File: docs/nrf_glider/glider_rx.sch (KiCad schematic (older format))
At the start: 8 parts

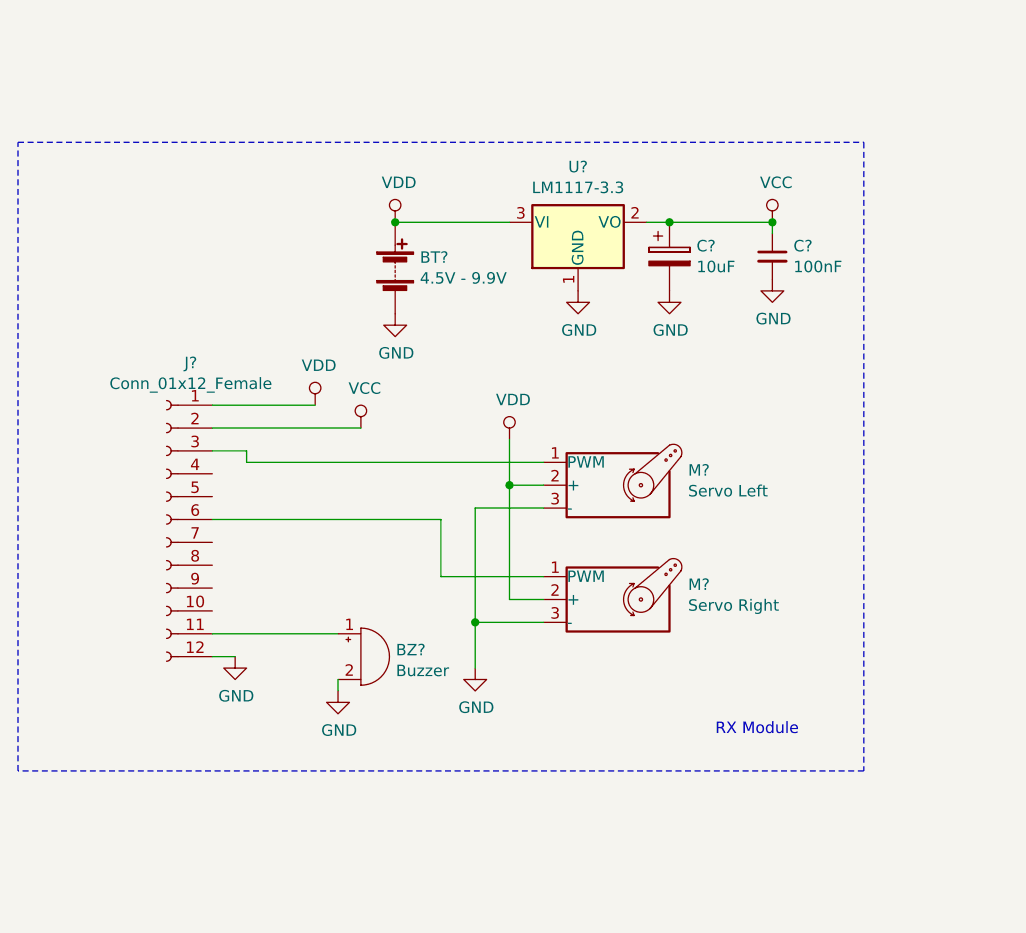
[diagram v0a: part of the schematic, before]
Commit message: added hierarchical sheets and labels
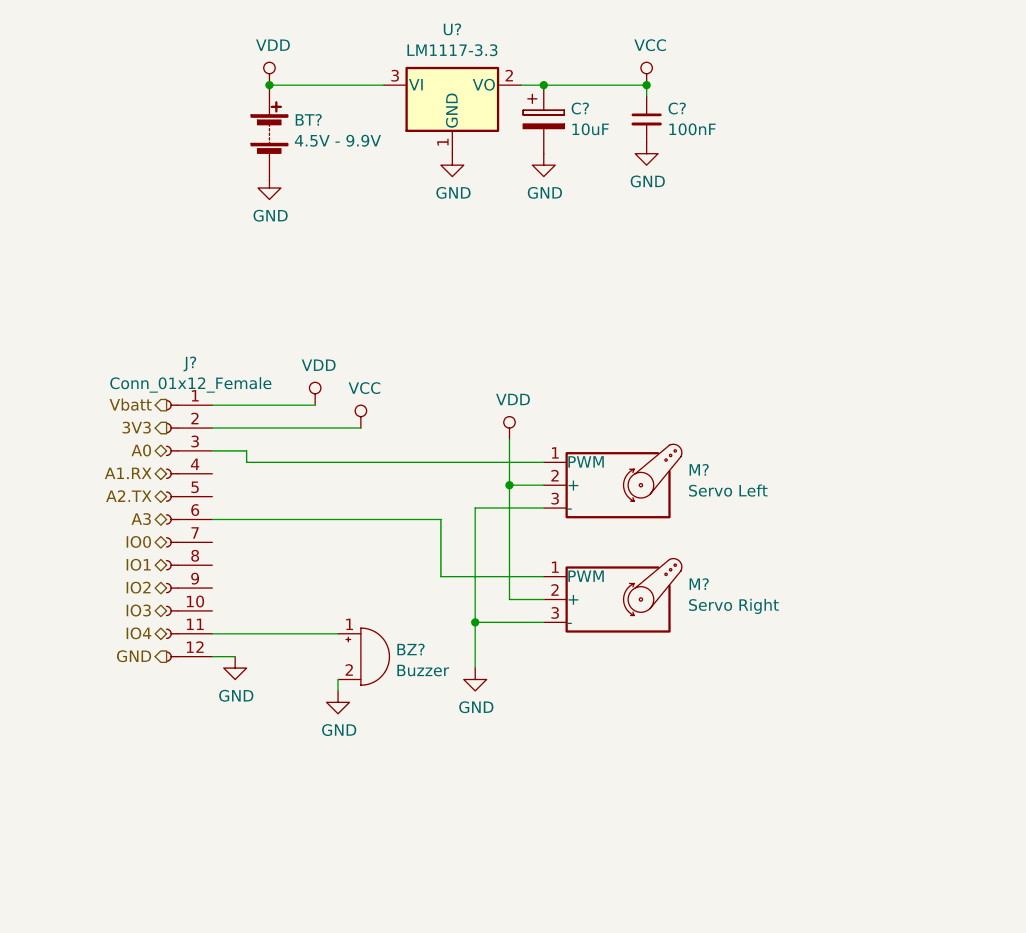
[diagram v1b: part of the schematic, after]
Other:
- note removed: "RX Module"
- moved on the sheet: BT?, C?, U?
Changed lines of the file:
@@
 $Descr A4 11693 8268
 encoding utf-8
-Sheet 4 4
+Sheet 1 5
 Title ""
 Date ""
@@
 L Regulator_Linear:LM1117-3.3 U?
 U 1 1 5BCECE85
-P 5050 2450
-F 0 "U?" H 5050 2692 50  0000 C CNN
-F 1 "LM1117-3.3" H 5050 2601 50  0000 C CNN
-F 2 "" H 5050 2450 50  0001 C CNN
-F 3 "http://www.ti.com/lit/ds/symlink/lm1117.pdf" H 5050 2450 50  0001 C CNN
-	1    5050 2450
+P 4500 1850
+F 0 "U?" H 4500 2092 50  0000 C CNN
+F 1 "LM1117-3.3" H 4500 2001 50  0000 C CNN
+F 2 "" H 4500 1850 50  0001 C CNN
+F 3 "http://www.ti.com/lit/ds/symlink/lm1117.pdf" H 4500 1850 50  0001 C CNN
+	1    4500 1850
 	1    0    0    -1
 $EndComp
@@
 L power:GND #PWR?
 U 1 1 5BCED801
-P 5050 2750
-F 0 "#PWR?" H 5050 2500 50  0001 C CNN
-F 1 "GND" H 5055 2577 50  0000 C CNN
-F 2 "" H 5050 2750 50  0001 C CNN
-F 3 "" H 5050 2750 50  0001 C CNN
-	1    5050 2750
+P 4500 2150
+F 0 "#PWR?" H 4500 1900 50  0001 C CNN
+F 1 "GND" H 4505 1977 50  0000 C CNN
+F 2 "" H 4500 2150 50  0001 C CNN
+F 3 "" H 4500 2150 50  0001 C CNN
+	1    4500 2150
 	1    0    0    -1
 $EndComp
@@
 L Device:Battery BT?
 U 1 1 5BCED8B9
-P 4250 2650
-F 0 "BT?" H 4358 2696 50  0000 L CNN
-F 1 "4.5V - 9.9V" H 4358 2605 50  0000 L CNN
-F 2 "Connector_PinHeader_2.54mm:PinHeader_1x02_P2.54mm_Vertical" V 4250 2710 50  0001 C CNN
-F 3 "~" V 4250 2710 50  0001 C CNN
-	1    4250 2650
-	1    0    0    -1
-$EndComp
-Wire Wire Line
-	4250 2450 4750 2450
+P 3700 2050
+F 0 "BT?" H 3808 2096 50  0000 L CNN
+F 1 "4.5V - 9.9V" H 3808 2005 50  0000 L CNN
+F 2 "Connector_PinHeader_2.54mm:PinHeader_1x02_P2.54mm_Vertical" V 3700 2110 50  0001 C CNN
+F 3 "~" V 3700 2110 50  0001 C CNN
+	1    3700 2050
+	1    0    0    -1
+$EndComp
+Wire Wire Line
+	3700 1850 4200 1850
 $Comp
 L power:GND #PWR?
 U 1 1 5BCED983
-P 4250 2850
-F 0 "#PWR?" H 4250 2600 50  0001 C CNN
-F 1 "GND" H 4255 2677 50  0000 C CNN
-F 2 "" H 4250 2850 50  0001 C CNN
-F 3 "" H 4250 2850 50  0001 C CNN
-	1    4250 2850
+P 3700 2250
+F 0 "#PWR?" H 3700 2000 50  0001 C CNN
+F 1 "GND" H 3705 2077 50  0000 C CNN
+F 2 "" H 3700 2250 50  0001 C CNN
+F 3 "" H 3700 2250 50  0001 C CNN
+	1    3700 2250
 	1    0    0    -1
 $EndComp
@@
 L power:VCC #PWR?
 U 1 1 5BCED9FA
-P 5900 2450
-F 0 "#PWR?" H 5900 2300 50  0001 C CNN
-F 1 "VCC" H 5917 2623 50  0000 C CNN
-F 2 "" H 5900 2450 50  0001 C CNN
-F 3 "" H 5900 2450 50  0001 C CNN
-	1    5900 2450
+P 5350 1850
+F 0 "#PWR?" H 5350 1700 50  0001 C CNN
+F 1 "VCC" H 5367 2023 50  0000 C CNN
+F 2 "" H 5350 1850 50  0001 C CNN
+F 3 "" H 5350 1850 50  0001 C CNN
+	1    5350 1850
 	1    0    0    -1
 $EndComp
@@
 L Device:C_Small C?
 U 1 1 5BCEDC62
-P 5900 2600
-F 0 "C?" H 5992 2646 50  0000 L CNN
-F 1 "100nF" H 5992 2555 50  0000 L CNN
-F 2 "Capacitor_THT:C_Disc_D5.0mm_W2.5mm_P5.00mm" H 5900 2600 50  0001 C CNN
-F 3 "~" H 5900 2600 50  0001 C CNN
-	1    5900 2600
+P 5350 2000
+F 0 "C?" H 5442 2046 50  0000 L CNN
+F 1 "100nF" H 5442 1955 50  0000 L CNN
+F 2 "Capacitor_THT:C_Disc_D5.0mm_W2.5mm_P5.00mm" H 5350 2000 50  0001 C CNN
+F 3 "~" H 5350 2000 50  0001 C CNN
+	1    5350 2000
 	1    0    0    -1
 $EndComp
@@
 L Device:CP C?
 U 1 1 5BCEDD9D
-P 5450 2600
-F 0 "C?" H 5568 2646 50  0000 L CNN
-F 1 "10uF" H 5568 2555 50  0000 L CNN
-F 2 "Capacitor_THT:CP_Radial_D8.0mm_P2.50mm" H 5488 2450 50  0001 C CNN
-F 3 "~" H 5450 2600 50  0001 C CNN
-	1    5450 2600
+P 4900 2000
+F 0 "C?" H 5018 2046 50  0000 L CNN
+F 1 "10uF" H 5018 1955 50  0000 L CNN
+F 2 "Capacitor_THT:CP_Radial_D8.0mm_P2.50mm" H 4938 1850 50  0001 C CNN
+F 3 "~" H 4900 2000 50  0001 C CNN
+	1    4900 2000
 	1    0    0    -1
 $EndComp
@@
 L power:GND #PWR?
 U 1 1 5BCEDF2F
-P 5450 2750
-F 0 "#PWR?" H 5450 2500 50  0001 C CNN
-F 1 "GND" H 5455 2577 50  0000 C CNN
-F 2 "" H 5450 2750 50  0001 C CNN
-F 3 "" H 5450 2750 50  0001 C CNN
-	1    5450 2750
+P 4900 2150
+F 0 "#PWR?" H 4900 1900 50  0001 C CNN
+F 1 "GND" H 4905 1977 50  0000 C CNN
+F 2 "" H 4900 2150 50  0001 C CNN
+F 3 "" H 4900 2150 50  0001 C CNN
+	1    4900 2150
 	1    0    0    -1
 $EndComp
@@
 L power:GND #PWR?
 U 1 1 5BCEDF6D
-P 5900 2700
-F 0 "#PWR?" H 5900 2450 50  0001 C CNN
-F 1 "GND" H 5905 2527 50  0000 C CNN
-F 2 "" H 5900 2700 50  0001 C CNN
-F 3 "" H 5900 2700 50  0001 C CNN
-	1    5900 2700
-	1    0    0    -1
-$EndComp
-Wire Wire Line
-	5350 2450 5450 2450
+P 5350 2100
+F 0 "#PWR?" H 5350 1850 50  0001 C CNN
+F 1 "GND" H 5355 1927 50  0000 C CNN
+F 2 "" H 5350 2100 50  0001 C CNN
+F 3 "" H 5350 2100 50  0001 C CNN
+	1    5350 2100
+	1    0    0    -1
+$EndComp
+Wire Wire Line
+	4800 1850 4900 1850
 $Comp
 L power:VDD #PWR?
 U 1 1 5BCF6415
-P 4250 2450
-F 0 "#PWR?" H 4250 2300 50  0001 C CNN
-F 1 "VDD" H 4267 2623 50  0000 C CNN
-F 2 "" H 4250 2450 50  0001 C CNN
-F 3 "" H 4250 2450 50  0001 C CNN
-	1    4250 2450
-	1    0    0    -1
-$EndComp
-Connection ~ 4250 2450
-Wire Wire Line
-	5900 2450 5900 2500
-Connection ~ 5900 2450
-Wire Wire Line
-	5450 2450 5900 2450
-Connection ~ 5450 2450
+P 3700 1850
+F 0 "#PWR?" H 3700 1700 50  0001 C CNN
+F 1 "VDD" H 3717 2023 50  0000 C CNN
+F 2 "" H 3700 1850 50  0001 C CNN
+F 3 "" H 3700 1850 50  0001 C CNN
+	1    3700 1850
+	1    0    0    -1
+$EndComp
+Connection ~ 3700 1850
+Wire Wire Line
+	5350 1850 5350 1900
+Connection ~ 5350 1850
+Wire Wire Line
+	4900 1850 5350 1850
+Connection ~ 4900 1850
 $Comp
 L Connector:Conn_01x12_Female J?
@@
 	1    0    0    -1
 $EndComp
-Wire Notes Line
-	2600 2100 6300 2100
-Wire Notes Line
-	6300 2100 6300 4850
-Wire Notes Line
-	6300 4850 2600 4850
-Wire Notes Line
-	2600 4850 2600 2100
-Text Notes 5650 4700 0    50   ~ 0
-RX Module
 Wire Wire Line
 	3450 3450 3600 3450
@@
 Text Notes 10300 7350 0    50   ~ 0
 created by Toby Kurien
+Text HLabel 3250 3250 0    50   Output ~ 0
+Vbatt
+Text HLabel 3250 3350 0    50   Output ~ 0
+3V3
+Text HLabel 3250 3450 0    50   BiDi ~ 0
+A0
+Text HLabel 3250 3550 0    50   BiDi ~ 0
+A1.RX
+Text HLabel 3250 3650 0    50   BiDi ~ 0
+A2.TX
+Text HLabel 3250 3750 0    50   BiDi ~ 0
+A3
+Text HLabel 3250 3850 0    50   BiDi ~ 0
+IO0
+Text HLabel 3250 3950 0    50   BiDi ~ 0
+IO1
+Text HLabel 3250 4050 0    50   BiDi ~ 0
+IO2
+Text HLabel 3250 4150 0    50   BiDi ~ 0
+IO3
+Text HLabel 3250 4250 0    50   BiDi ~ 0
+IO4
+Text HLabel 3250 4350 0    50   Output ~ 0
+GND
 $EndSCHEMATC

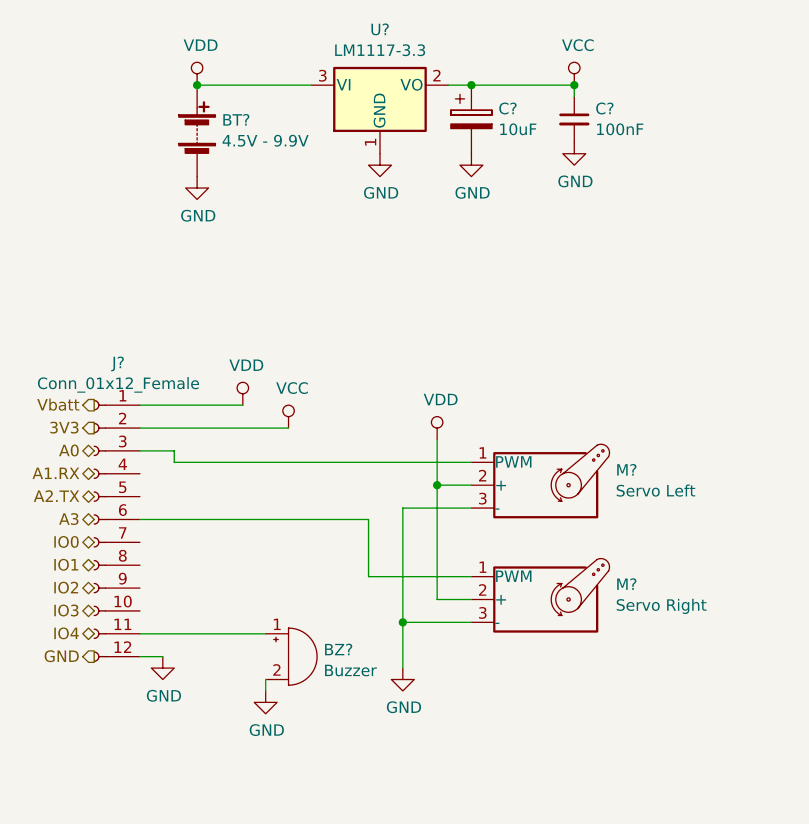
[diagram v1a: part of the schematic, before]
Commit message: remove and ignore bak files
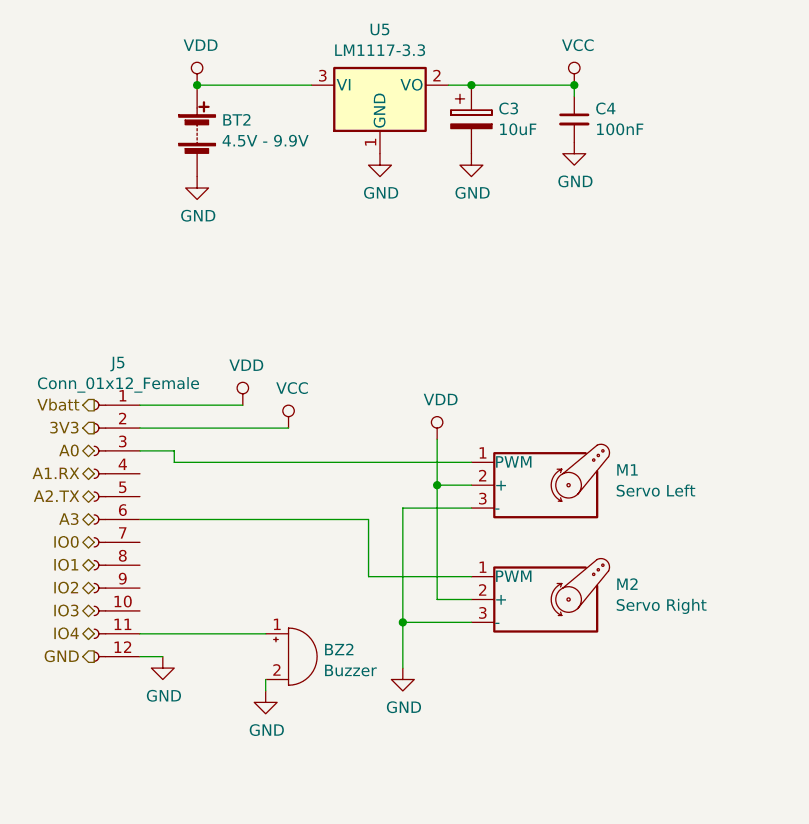
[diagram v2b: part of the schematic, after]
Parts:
- gave numbers to parts that had none: 8
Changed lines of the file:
@@
 $EndDescr
 $Comp
-L Regulator_Linear:LM1117-3.3 U?
+L Regulator_Linear:LM1117-3.3 U5
 U 1 1 5BCECE85
 P 4500 1850
-F 0 "U?" H 4500 2092 50  0000 C CNN
+F 0 "U5" H 4500 2092 50  0000 C CNN
 F 1 "LM1117-3.3" H 4500 2001 50  0000 C CNN
 F 2 "" H 4500 1850 50  0001 C CNN
@@
 $EndComp
 $Comp
-L power:GND #PWR?
+L power:GND #PWR0129
 U 1 1 5BCED801
 P 4500 2150
-F 0 "#PWR?" H 4500 1900 50  0001 C CNN
+F 0 "#PWR0129" H 4500 1900 50  0001 C CNN
 F 1 "GND" H 4505 1977 50  0000 C CNN
 F 2 "" H 4500 2150 50  0001 C CNN
@@
 $EndComp
 $Comp
-L Device:Battery BT?
+L Device:Battery BT2
 U 1 1 5BCED8B9
 P 3700 2050
-F 0 "BT?" H 3808 2096 50  0000 L CNN
+F 0 "BT2" H 3808 2096 50  0000 L CNN
 F 1 "4.5V - 9.9V" H 3808 2005 50  0000 L CNN
 F 2 "Connector_PinHeader_2.54mm:PinHeader_1x02_P2.54mm_Vertical" V 3700 2110 50  0001 C CNN
@@
 	3700 1850 4200 1850
 $Comp
-L power:GND #PWR?
+L power:GND #PWR0130
 U 1 1 5BCED983
 P 3700 2250
-F 0 "#PWR?" H 3700 2000 50  0001 C CNN
+F 0 "#PWR0130" H 3700 2000 50  0001 C CNN
 F 1 "GND" H 3705 2077 50  0000 C CNN
 F 2 "" H 3700 2250 50  0001 C CNN
@@
 $EndComp
 $Comp
-L power:VCC #PWR?
+L power:VCC #PWR0131
 U 1 1 5BCED9FA
 P 5350 1850
-F 0 "#PWR?" H 5350 1700 50  0001 C CNN
+F 0 "#PWR0131" H 5350 1700 50  0001 C CNN
 F 1 "VCC" H 5367 2023 50  0000 C CNN
 F 2 "" H 5350 1850 50  0001 C CNN
@@
 $EndComp
 $Comp
-L Device:C_Small C?
+L Device:C_Small C4
 U 1 1 5BCEDC62
 P 5350 2000
-F 0 "C?" H 5442 2046 50  0000 L CNN
+F 0 "C4" H 5442 2046 50  0000 L CNN
 F 1 "100nF" H 5442 1955 50  0000 L CNN
 F 2 "Capacitor_THT:C_Disc_D5.0mm_W2.5mm_P5.00mm" H 5350 2000 50  0001 C CNN
@@
 $EndComp
 $Comp
-L Device:CP C?
+L Device:CP C3
 U 1 1 5BCEDD9D
 P 4900 2000
-F 0 "C?" H 5018 2046 50  0000 L CNN
+F 0 "C3" H 5018 2046 50  0000 L CNN
 F 1 "10uF" H 5018 1955 50  0000 L CNN
 F 2 "Capacitor_THT:CP_Radial_D8.0mm_P2.50mm" H 4938 1850 50  0001 C CNN
@@
 $EndComp
 $Comp
-L power:GND #PWR?
+L power:GND #PWR0132
 U 1 1 5BCEDF2F
 P 4900 2150
-F 0 "#PWR?" H 4900 1900 50  0001 C CNN
+F 0 "#PWR0132" H 4900 1900 50  0001 C CNN
 F 1 "GND" H 4905 1977 50  0000 C CNN
 F 2 "" H 4900 2150 50  0001 C CNN
@@
 $EndComp
 $Comp
-L power:GND #PWR?
+L power:GND #PWR0133
 U 1 1 5BCEDF6D
 P 5350 2100
-F 0 "#PWR?" H 5350 1850 50  0001 C CNN
+F 0 "#PWR0133" H 5350 1850 50  0001 C CNN
 F 1 "GND" H 5355 1927 50  0000 C CNN
 F 2 "" H 5350 2100 50  0001 C CNN
@@
 	4800 1850 4900 1850
 $Comp
-L power:VDD #PWR?
+L power:VDD #PWR0134
 U 1 1 5BCF6415
 P 3700 1850
-F 0 "#PWR?" H 3700 1700 50  0001 C CNN
+F 0 "#PWR0134" H 3700 1700 50  0001 C CNN
 F 1 "VDD" H 3717 2023 50  0000 C CNN
 F 2 "" H 3700 1850 50  0001 C CNN
@@
 Connection ~ 4900 1850
 $Comp
-L Connector:Conn_01x12_Female J?
+L Connector:Conn_01x12_Female J5
 U 1 1 5BD137AB
 P 3250 3750
-F 0 "J?" H 3144 4435 50  0000 C CNN
+F 0 "J5" H 3144 4435 50  0000 C CNN
 F 1 "Conn_01x12_Female" H 3144 4344 50  0000 C CNN
 F 2 "Connector_PinHeader_2.54mm:PinHeader_1x12_P2.54mm_Vertical" H 3250 3750 50  0001 C CNN
@@
 $EndComp
 $Comp
-L power:VDD #PWR?
+L power:VDD #PWR0135
 U 1 1 5BD1962D
 P 3900 3250
-F 0 "#PWR?" H 3900 3100 50  0001 C CNN
+F 0 "#PWR0135" H 3900 3100 50  0001 C CNN
 F 1 "VDD" H 3917 3423 50  0000 C CNN
 F 2 "" H 3900 3250 50  0001 C CNN
@@
 	3900 3250 3450 3250
 $Comp
-L power:VCC #PWR?
+L power:VCC #PWR0136
 U 1 1 5BD1B4CC
 P 4100 3350
-F 0 "#PWR?" H 4100 3200 50  0001 C CNN
+F 0 "#PWR0136" H 4100 3200 50  0001 C CNN
 F 1 "VCC" H 4117 3523 50  0000 C CNN
 F 2 "" H 4100 3350 50  0001 C CNN
@@
 	3450 3350 4100 3350
 $Comp
-L power:GND #PWR?
+L power:GND #PWR0137
 U 1 1 5BD1F411
 P 3550 4350
-F 0 "#PWR?" H 3550 4100 50  0001 C CNN
+F 0 "#PWR0137" H 3550 4100 50  0001 C CNN
 F 1 "GND" H 3555 4177 50  0000 C CNN
 F 2 "" H 3550 4350 50  0001 C CNN
@@
 	3450 4350 3550 4350
 $Comp
-L Motor:Motor_Servo M?
+L Motor:Motor_Servo M1
 U 1 1 5BD298F1
 P 5200 3600
-F 0 "M?" H 5531 3665 50  0000 L CNN
+F 0 "M1" H 5531 3665 50  0000 L CNN
 F 1 "Servo Left" H 5531 3574 50  0000 L CNN
 F 2 "Connector_PinHeader_2.54mm:PinHeader_1x03_P2.54mm_Vertical" H 5200 3410 50  0001 C CNN
@@
 $EndComp
 $Comp
-L Motor:Motor_Servo M?
+L Motor:Motor_Servo M2
 U 1 1 5BD29998
 P 5200 4100
-F 0 "M?" H 5531 4165 50  0000 L CNN
+F 0 "M2" H 5531 4165 50  0000 L CNN
 F 1 "Servo Right" H 5531 4074 50  0000 L CNN
 F 2 "Connector_PinHeader_2.54mm:PinHeader_1x03_P2.54mm_Vertical" H 5200 3910 50  0001 C CNN
@@
 $EndComp
 $Comp
-L Device:Buzzer BZ?
+L Device:Buzzer BZ2
 U 1 1 5BD29AB3
 P 4100 4350
-F 0 "BZ?" H 4253 4379 50  0000 L CNN
+F 0 "BZ2" H 4253 4379 50  0000 L CNN
 F 1 "Buzzer" H 4253 4288 50  0000 L CNN
 F 2 "Buzzer_Beeper:Buzzer_15x7.5RM7.6" V 4075 4450 50  0001 C CNN
@@
 	4450 4000 4900 4000
 $Comp
-L power:VDD #PWR?
+L power:VDD #PWR0138
 U 1 1 5BD6892B
 P 4750 3400
-F 0 "#PWR?" H 4750 3250 50  0001 C CNN
+F 0 "#PWR0138" H 4750 3250 50  0001 C CNN
 F 1 "VDD" H 4767 3573 50  0000 C CNN
 F 2 "" H 4750 3400 50  0001 C CNN
@@
 Connection ~ 4750 3600
 $Comp
-L power:GND #PWR?
+L power:GND #PWR0139
 U 1 1 5BD6F7A2
 P 4600 4400
-F 0 "#PWR?" H 4600 4150 50  0001 C CNN
+F 0 "#PWR0139" H 4600 4150 50  0001 C CNN
 F 1 "GND" H 4605 4227 50  0000 C CNN
 F 2 "" H 4600 4400 50  0001 C CNN
@@
 	3450 4250 4000 4250
 $Comp
-L power:GND #PWR?
+L power:GND #PWR0140
 U 1 1 5BD8512D
 P 4000 4500
-F 0 "#PWR?" H 4000 4250 50  0001 C CNN
+F 0 "#PWR0140" H 4000 4250 50  0001 C CNN
 F 1 "GND" H 4005 4327 50  0000 C CNN
 F 2 "" H 4000 4500 50  0001 C CNN
